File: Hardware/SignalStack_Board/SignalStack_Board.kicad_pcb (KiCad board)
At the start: 2 copper layers, 69.6 x 80.3 mm, 78 parts, among them J2 RJ45_LED_Shielded, J3 Molex_uF_SV_06, Q1 SI4156DY, Q2 SI4156DY, Q3 SI4156DY, Q4 SI4156DY, Q5 SI4156DY, Q6 SI4156DY, Q7 SI4156DY, Q8 SI4156DY, Q9 Q_PMOS_DGS, SW1 SW_Push, SW2 SW_Push, U1 OKI, U10 74LVC2G04, U2 SMAJ12CA, U3 Teensy4.1_DEV-16771, U4 TSR_1-2450, U5 IRS2005S, U6 IRS2005S, U7 74LVC2G04, U8 IRS2005S, U9 IRS2005S

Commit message: Rev3 schematic
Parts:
- added REF**: Arduino_UNO_R3, Module:Arduino_UNO_R3, B.Cu at (90.7, 106.6)
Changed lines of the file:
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@@
       ) (layer "B.SilkS") (width 0) (fill solid))
+  )
+  (footprint "Module:Arduino_UNO_R3" (layer "B.Cu")
+    (at 90.678 106.553 90)
+    (descr "Arduino UNO R3, http://www.mouser.com/pdfdocs/Gravitech_Arduino_Nano3_0.pdf")
+    (tags "Arduino UNO R3")
+    (attr through_hole)
+    (fp_text reference "REF**" (at 1.27 3.81 90) (layer "B.SilkS")
+      (effects (font (size 1 1) (thickness 0.15)) (justify mirror))
+    )
+    (fp_text value "Arduino_UNO_R3" (at 0 -22.86 90) (layer "B.Fab")
+      (effects (font (size 1 1) (thickness 0.15)) (justify mirror))
+    )
+    (fp_text user "${REFERENCE}" (at 0 -20.32 90) (layer "B.Fab")
+      (effects (font (size 1 1) (thickness 0.15)) (justify mirror))
+    )
+    (fp_line (start -28.07 -50.93) (end 36.58 -50.93) (layer "B.SilkS") (width 0.12))
+    (fp_line (start -28.07 -9.65) (end -28.07 -29.72) (layer "B.SilkS") (width 0.12))
+    (fp_line (start 38.23 -49.28) (end 38.23 -37.85) (layer "B.SilkS") (width 0.12))
+    (fp_line (start -29.97 -9.65) (end -28.07 -9.65) (layer "B.SilkS") (width 0.12))
+    (fp_line (start -34.42 -41.4) (end -28.07 -41.4) (layer "B.SilkS") (width 0.12))
+    (fp_line (start -28.07 -29.72) (end -34.42 -29.72) (layer "B.SilkS") (width 0.12))
+    (fp_line (start -34.42 -29.72) (end -34.42 -41.4) (layer "B.SilkS") (width 0.12))
+    (fp_line (start -28.07 -0.51) (end -29.97 -0.51) (layer "B.SilkS") (width 0.12))
+    (fp_line (start 38.23 2.67) (end -28.07 2.67) (layer "B.SilkS") (width 0.12))
+    (fp_line (start 38.23 -37.85) (end 40.77 -35.31) (layer "B.SilkS") (width 0.12))
+    (fp_line (start -29.97 -0.51) (end -29.97 -9.65) (layer "B.SilkS") (width 0.12))
+    (fp_line (start 40.77 -35.31) (end 40.77 -2.54) (layer "B.SilkS") (width 0.12))
+    (fp_line (start -28.07 -41.4) (end -28.07 -50.93) (layer "B.SilkS") (width 0.12))
+    (fp_line (start -28.07 2.67) (end -28.07 -0.51) (layer "B.SilkS") (width 0.12))
+    (fp_line (start 36.58 -50.93) (end 38.23 -49.28) (layer "B.SilkS") (width 0.12))
+    (fp_line (start 38.23 0) (end 38.23 2.67) (layer "B.SilkS") (width 0.12))
+    (fp_line (start 40.77 -2.54) (end 38.23 0) (layer "B.SilkS") (width 0.12))
+    (fp_line (start -30.1 -9.78) (end -30.1 -0.38) (layer "B.CrtYd") (width 0.05))
+    (fp_line (start -28.19 -9.78) (end -30.1 -9.78) (layer "B.CrtYd") (width 0.05))
+    (fp_line (start -28.19 2.79) (end 38.35 2.79) (layer "B.CrtYd") (width 0.05))
+    (fp_line (start 40.89 -35.31) (end 38.35 -37.85) (layer "B.CrtYd") (width 0.05))
+    (fp_line (start -28.19 -51.05) (end -28.19 -41.53) (layer "B.CrtYd") (width 0.05))
+    (fp_line (start -28.19 -0.38) (end -28.19 2.79) (layer "B.CrtYd") (width 0.05))
+    (fp_line (start -28.19 -29.59) (end -28.19 -9.78) (layer "B.CrtYd") (width 0.05))
+    (fp_line (start -34.54 -41.53) (end -34.54 -29.59) (layer "B.CrtYd") (width 0.05))
+    (fp_line (start -30.1 -0.38) (end -28.19 -0.38) (layer "B.CrtYd") (width 0.05))
+    (fp_line (start -28.19 -41.53) (end -34.54 -41.53) (layer "B.CrtYd") (width 0.05))
+    (fp_line (start 36.58 -51.05) (end -28.19 -51.05) (layer "B.CrtYd") (width 0.05))
+    (fp_line (start 38.35 -37.85) (end 38.35 -49.28) (layer "B.CrtYd") (width 0.05))
+    (fp_line (start 38.35 2.79) (end 38.35 0) (layer "B.CrtYd") (width 0.05))
+    (fp_line (start -34.54 -29.59) (end -28.19 -29.59) (layer "B.CrtYd") (width 0.05))
+    (fp_line (start 38.35 -49.28) (end 36.58 -51.05) (layer "B.CrtYd") (width 0.05))
+    (fp_line (start 40.89 -2.54) (end 40.89 -35.31) (layer "B.CrtYd") (width 0.05))
+    (fp_line (start 38.35 0) (end 40.89 -2.54) (layer "B.CrtYd") (width 0.05))
+    (fp_line (start 38.1 2.54) (end 38.1 0) (layer "B.Fab") (width 0.1))
+    (fp_line (start 40.64 -2.54) (end 40.64 -35.31) (layer "B.Fab") (width 0.1))
+    (fp_line (start -29.84 -0.64) (end -16.51 -0.64) (layer "B.Fab") (width 0.1))
+    (fp_line (start -16.51 -9.53) (end -29.84 -9.53) (layer "B.Fab") (width 0.1))
+    (fp_line (start -18.41 -29.84) (end -18.41 -41.27) (layer "B.Fab") (width 0.1))
+    (fp_line (start -29.84 -9.53) (end -29.84 -0.64) (layer "B.Fab") (width 0.1))
+    (fp_line (start 36.58 -50.8) (end -27.94 -50.8) (layer "B.Fab") (width 0.1))
+    (fp_line (start -16.51 -0.64) (end -16.51 -9.53) (layer "B.Fab") (width 0.1))
+    (fp_line (start -27.94 -50.8) (end -27.94 2.54) (layer "B.Fab") (width 0.1))
+    (fp_line (start -18.41 -41.27) (end -34.29 -41.27) (layer "B.Fab") (width 0.1))
+    (fp_line (start 38.1 -37.85) (end 38.1 -49.28) (layer "B.Fab") (width 0.1))
+    (fp_line (start 38.1 -49.28) (end 36.58 -50.8) (layer "B.Fab") (width 0.1))
+    (fp_line (start 38.1 0) (end 40.64 -2.54) (layer "B.Fab") (width 0.1))
+    (fp_line (start -34.29 -41.27) (end -34.29 -29.84) (layer "B.Fab") (width 0.1))
+    (fp_line (start 40.64 -35.31) (end 38.1 -37.85) (layer "B.Fab") (width 0.1))
+    (fp_line (start -27.94 2.54) (end 38.1 2.54) (layer "B.Fab") (width 0.1))
+    (fp_line (start -34.29 -29.84) (end -18.41 -29.84) (layer "B.Fab") (width 0.1))
+    (pad "1" thru_hole rect (at 0 0) (size 1.6 1.6) (drill 1) (layers *.Cu *.Mask))
+    (pad "2" thru_hole oval (at 2.54 0) (size 1.6 1.6) (drill 1) (layers *.Cu *.Mask))
+    (pad "3" thru_hole oval (at 5.08 0) (size 1.6 1.6) (drill 1) (layers *.Cu *.Mask))
+    (pad "4" thru_hole oval (at 7.62 0) (size 1.6 1.6) (drill 1) (layers *.Cu *.Mask))
+    (pad "5" thru_hole oval (at 10.16 0) (size 1.6 1.6) (drill 1) (layers *.Cu *.Mask))
+    (pad "6" thru_hole oval (at 12.7 0) (size 1.6 1.6) (drill 1) (layers *.Cu *.Mask))
+    (pad "7" thru_hole oval (at 15.24 0) (size 1.6 1.6) (drill 1) (layers *.Cu *.Mask))
+    (pad "8" thru_hole oval (at 17.78 0) (size 1.6 1.6) (drill 1) (layers *.Cu *.Mask))
+    (pad "9" thru_hole oval (at 22.86 0) (size 1.6 1.6) (drill 1) (layers *.Cu *.Mask))
+    (pad "10" thru_hole oval (at 25.4 0) (size 1.6 1.6) (drill 1) (layers *.Cu *.Mask))
+    (pad "11" thru_hole oval (at 27.94 0) (size 1.6 1.6) (drill 1) (layers *.Cu *.Mask))
+    (pad "12" thru_hole oval (at 30.48 0) (size 1.6 1.6) (drill 1) (layers *.Cu *.Mask))
+    (pad "13" thru_hole oval (at 33.02 0) (size 1.6 1.6) (drill 1) (layers *.Cu *.Mask))
+    (pad "14" thru_hole oval (at 35.56 0) (size 1.6 1.6) (drill 1) (layers *.Cu *.Mask))
+    (pad "15" thru_hole oval (at 35.56 -48.26) (size 1.6 1.6) (drill 1) (layers *.Cu *.Mask))
+    (pad "16" thru_hole oval (at 33.02 -48.26) (size 1.6 1.6) (drill 1) (layers *.Cu *.Mask))
+    (pad "17" thru_hole oval (at 30.48 -48.26) (size 1.6 1.6) (drill 1) (layers *.Cu *.Mask))
+    (pad "18" thru_hole oval (at 27.94 -48.26) (size 1.6 1.6) (drill 1) (layers *.Cu *.Mask))
+    (pad "19" thru_hole oval (at 25.4 -48.26) (size 1.6 1.6) (drill 1) (layers *.Cu *.Mask))
+    (pad "20" thru_hole oval (at 22.86 -48.26) (size 1.6 1.6) (drill 1) (layers *.Cu *.Mask))
+    (pad "21" thru_hole oval (at 20.32 -48.26) (size 1.6 1.6) (drill 1) (layers *.Cu *.Mask))
+    (pad "22" thru_hole oval (at 17.78 -48.26) (size 1.6 1.6) (drill 1) (layers *.Cu *.Mask))
+    (pad "23" thru_hole oval (at 13.72 -48.26) (size 1.6 1.6) (drill 1) (layers *.Cu *.Mask))
+    (pad "24" thru_hole oval (at 11.18 -48.26) (size 1.6 1.6) (drill 1) (layers *.Cu *.Mask))
+    (pad "25" thru_hole oval (at 8.64 -48.26) (size 1.6 1.6) (drill 1) (layers *.Cu *.Mask))
+    (pad "26" thru_hole oval (at 6.1 -48.26) (size 1.6 1.6) (drill 1) (layers *.Cu *.Mask))
+    (pad "27" thru_hole oval (at 3.56 -48.26) (size 1.6 1.6) (drill 1) (layers *.Cu *.Mask))
+    (pad "28" thru_hole oval (at 1.02 -48.26) (size 1.6 1.6) (drill 1) (layers *.Cu *.Mask))
+    (pad "29" thru_hole oval (at -1.52 -48.26) (size 1.6 1.6) (drill 1) (layers *.Cu *.Mask))
+    (pad "30" thru_hole oval (at -4.06 -48.26) (size 1.6 1.6) (drill 1) (layers *.Cu *.Mask))
+    (pad "31" thru_hole oval (at -6.6 -48.26) (size 1.6 1.6) (drill 1) (layers *.Cu *.Mask))
+    (pad "32" thru_hole oval (at -9.14 -48.26) (size 1.6 1.6) (drill 1) (layers *.Cu *.Mask))
+    (model "${KICAD6_3DMODEL_DIR}/Module.3dshapes/Arduino_UNO_R3.wrl"
+      (offset (xyz 0 0 0))
+      (scale (xyz 1 1 1))
+      (rotate (xyz 0 0 0))
+    )
   )
   (footprint "MRDT_Connectors:Square_Anderson_2_H_Side_By_Side" (layer "B.Cu")

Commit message: Made Rev3 layout
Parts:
- removed C6: 0.1uF, Capacitor_SMD:C_0603_1608Metric_Pad1.08x0.95mm_HandSolder
- removed the G*** at (159.8, 127.8)
- removed the G*** at (165.4, 104.9)
- removed J2: RJ45_LED_Shielded, MRDT_Connectors:RJ45_Teensy
- removed J3: Molex_uF_SV_06, Connector_Molex:Molex_SL_171971-0006_1x06_P2.54mm_Vertical
- removed R19, R20: 4.7k, Resistor_SMD:R_0603_1608Metric_Pad0.98x0.95mm_HandSolder
- removed REF**: Arduino_UNO_R3, Module:Arduino_UNO_R3
- removed U3: Teensy4.1_DEV-16771, MRDT_Shields:Teensy_4_1_Ethernet
- removed V4: Via, MRDT_Drill_Holes:4_40_Hole_Corner
- added A1: Arduino_UNO_R3, Module:Arduino_UNO_R3, F.Cu at (203.2, 34.3)
- added G***: LOGO, MRDT_Silkscreens:z_sig_Grant_Brinker_30mmx7.3, F.Cu at (202.6, 102.2)
- added G***: LOGO, MRDT_Silkscreens:zz_Helios_Logo_Short_3inx1.4in, F.Cu at (204.5, 61.6)
- C3: value 0.1uF -> 100uF; footprint Capacitor_SMD:C_0603_1608Metric_Pad1.08x0.95mm_HandSolder -> Capacitor_THT:CP_Radial_D6.3mm_P2.50mm
- C4: value 10uF -> 220uF; footprint Capacitor_SMD:C_0603_1608Metric_Pad1.08x0.95mm_HandSolder -> Capacitor_THT:CP_Radial_D6.3mm_P2.50mm
- C5: value 22uF -> 470uF; footprint Capacitor_SMD:C_0603_1608Metric_Pad1.08x0.95mm_HandSolder -> Capacitor_THT:CP_Radial_D10.0mm_P2.50mm
- U2: value SMAJ12CA -> Raspberry_Pi; footprint MRDT_Actives:DO-214AC -> MRDT_Shields:RaspberryPi_THT_BOTTOM
- moved V1 134.9 mm to (243.8, 108.0), turned to 90 degrees
- moved V3 120.5 mm to (125.7, 31.8), turned to -90 degrees
- moved C2 80.0 mm to (128.7, 59.3)
- moved V2 75.2 mm to (125.7, 108.0), turned to 0 degrees
- moved Conn1 69.5 mm to (231.8, 89.2)
- moved U1 60.4 mm to (134.6, 55.6), turned to 180 degrees
- moved D1 60.3 mm to (153.0, 47.8), turned to 180 degrees
- moved R1 59.7 mm to (149.2, 47.8), turned to 0 degrees
- moved Q9 59.1 mm to (221.3, 96.5), turned to 0 degrees
- moved U4 55.3 mm to (142.2, 50.8)
- moved C5 54.7 mm to (204.5, 92.7), turned to 90 degrees
- moved D3 54.7 mm to (153.0, 50.5), turned to 180 degrees
- moved C1 54.4 mm to (135.5, 59.3), turned to 0 degrees
- moved R3 54.1 mm to (149.2, 50.5), turned to 0 degrees
- moved D2 49.2 mm to (153.0, 53.3), turned to 180 degrees
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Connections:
- C3 pad 1: Net-(C3-Pad1) -> +12V
- C4 pad 1: Net-(C3-Pad1) -> +12V
- C5 pad 1: Net-(C3-Pad1) -> +12V
- Conn1 pad 2: Net-(C3-Pad1) -> Net-(Conn1-Pad2)
- D12 pad 1: +12V -> Net-(D12-Pad2)
- D12 pad 2: Net-(D12-Pad2) -> (no net)
- D12 pad 3: (no net) -> +12V
- Q9 pad 2: Net-(C3-Pad1) -> Net-(Conn1-Pad2)
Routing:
- net +3V3: track 293.6 -> 158.8 mm, vias 7 -> 4
- net GPS_TX1: track 0.00 -> 104.0 mm
- net Coil1_FWD: track 19.6 -> 117.8 mm
- net GPS_RX1: track 0.00 -> 91.6 mm
- net Coil2_RVS: track 16.5 -> 98.3 mm
- net Coil2_FWD: track 19.3 -> 96.3 mm
- net Coil1_RVS: track 19.4 -> 89.2 mm, vias 0 -> 2
- net I2C SCL: track 56.4 -> 0.00 mm, vias 1 -> 0
- net I2C SDA: track 53.3 -> 0.00 mm, vias 1 -> 0
- net +5V: track 53.9 -> 90.7 mm
- net /RX-: track 31.4 -> 0.00 mm
- net /RX+: track 31.4 -> 0.00 mm
- net /LED: track 31.1 -> 0.00 mm
- net /TX-: track 23.5 -> 0.00 mm
- net /TX+: track 23.5 -> 0.00 mm
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- added copper zone on F.Cu, net Net-(Conn1-Pad2)
- removed copper zone on F.Cu, net Net-(C3-Pad1)
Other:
- board size 69.6 x 80.3 mm -> 118.1 x 76.2 mm
- board text added: "3.3V"
- board text added: "Signal Stack Board, Rev3 Mars Rover Design Team Missouri S&T, 2023 Grant Brinker"
- board text removed: "3V3"
- board text removed: "Signal Stack Board, Rev 2 Mars Rover Design Team Missouri S&T, 2023 Grant Brinker"

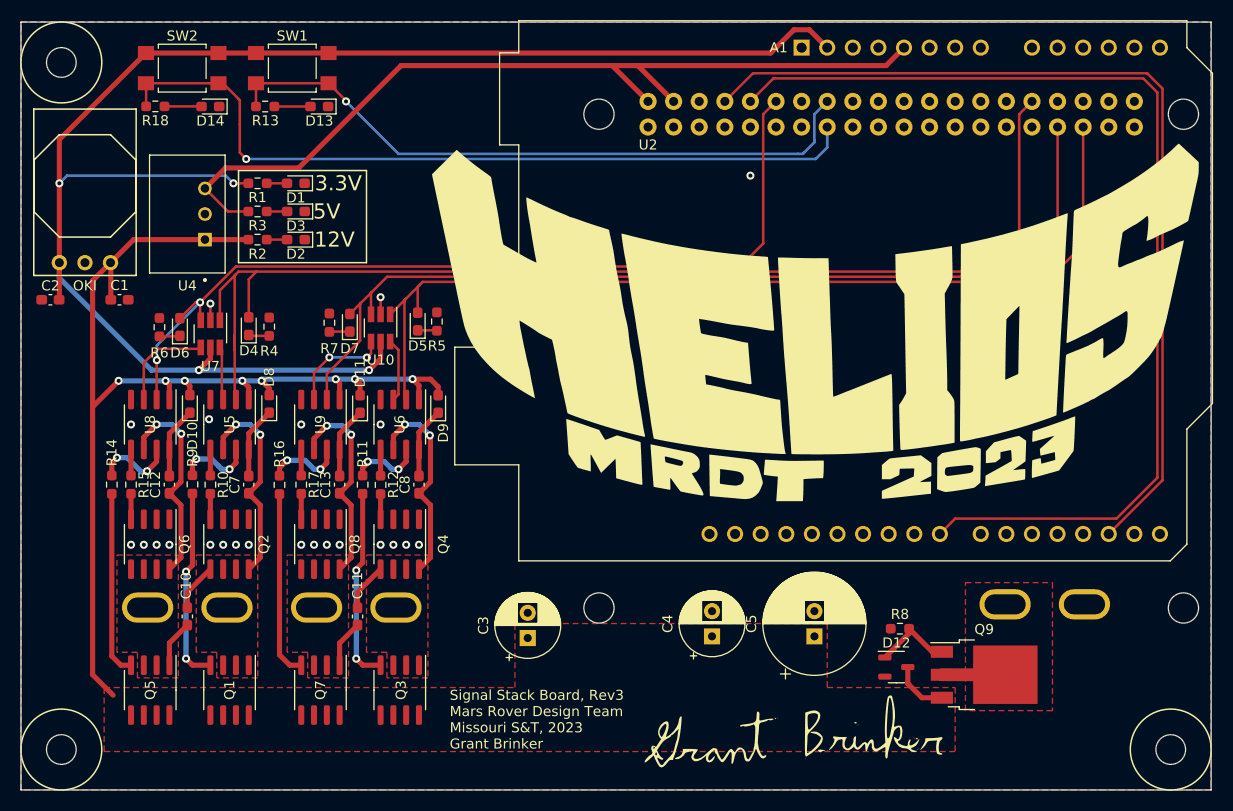
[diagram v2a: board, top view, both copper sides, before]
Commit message: Fixed edge cuts
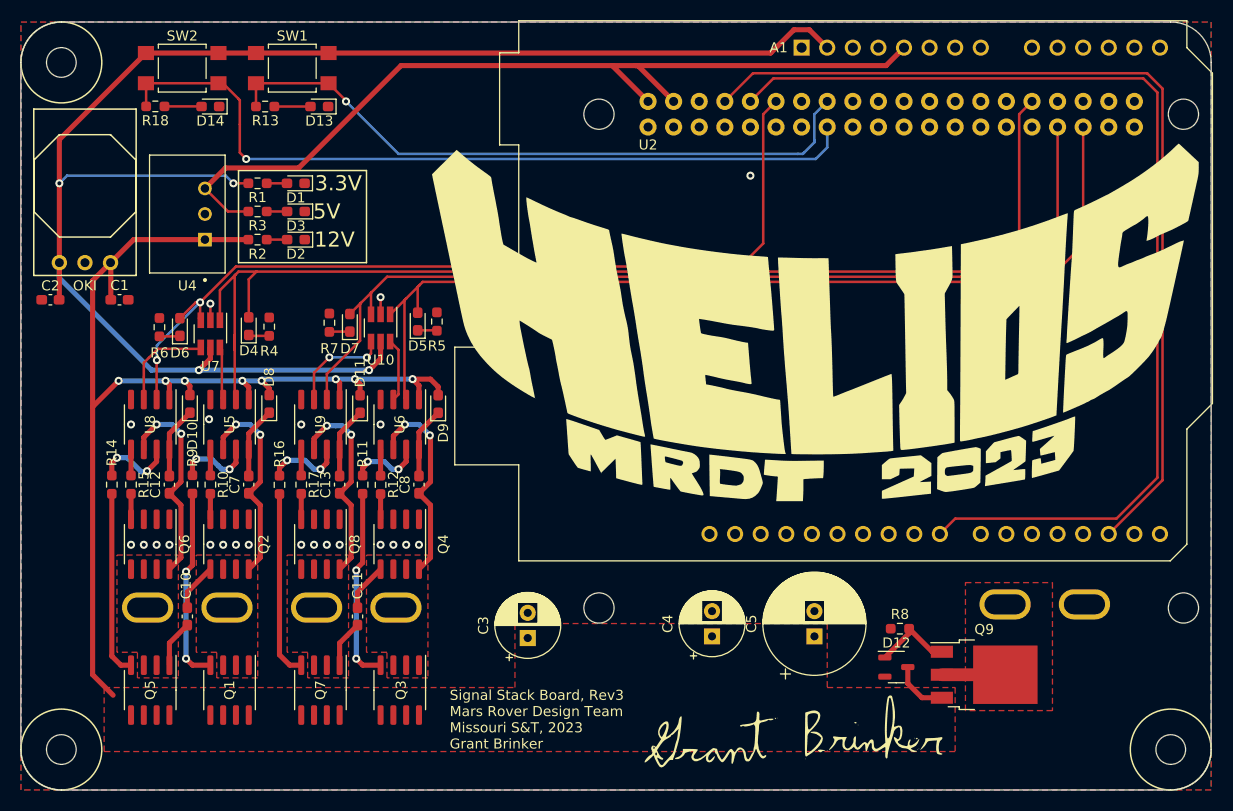
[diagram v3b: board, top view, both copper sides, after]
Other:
- outline, holes or cut-outs redrawn
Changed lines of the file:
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@@
   )
   (gr_rect (start 147.32 55.626) (end 160.02 46.482) (layer "F.SilkS") (width 0.15) (fill none))
-  (gr_rect (start 125.73 31.75) (end 243.84 107.95) (layer "Edge.Cuts") (width 0.1) (fill none))
+  (gr_line (start 243.84 103.9368) (end 243.847039 35.756161) (layer "Edge.Cuts") (width 0.1))
+  (gr_line (start 129.736161 31.742961) (end 239.833839 31.742961) (layer "Edge.Cuts") (width 0.1))
+  (gr_line (start 125.722961 103.943839) (end 125.722961 35.756161) (layer "Edge.Cuts") (width 0.1))
+  (gr_line (start 239.8268 107.95) (end 129.736161 107.957039) (layer "Edge.Cuts") (width 0.1))
+  (gr_arc (start 125.722961 35.756161) (mid 126.8984 32.9184) (end 129.736161 31.742961) (layer "Edge.Cuts") (width 0.1))
+  (gr_arc (start 239.833839 31.742961) (mid 242.6716 32.9184) (end 243.847039 35.756161) (layer "Edge.Cuts") (width 0.1))
+  (gr_arc (start 129.736161 107.957039) (mid 126.8984 106.7816) (end 125.722961 103.943839) (layer "Edge.Cuts") (width 0.1))
+  (gr_arc (start 243.84 103.9368) (mid 242.664561 106.774561) (end 239.8268 107.95) (layer "Edge.Cuts") (width 0.1))
   (gr_text "Signal Stack Board, Rev3\nMars Rover Design Team\nMissouri S&T, 2023\nGrant Brinker" (at 168.275 100.965) (layer "F.SilkS")
     (effects (font (size 1 1) (thickness 0.15)) (justify left))

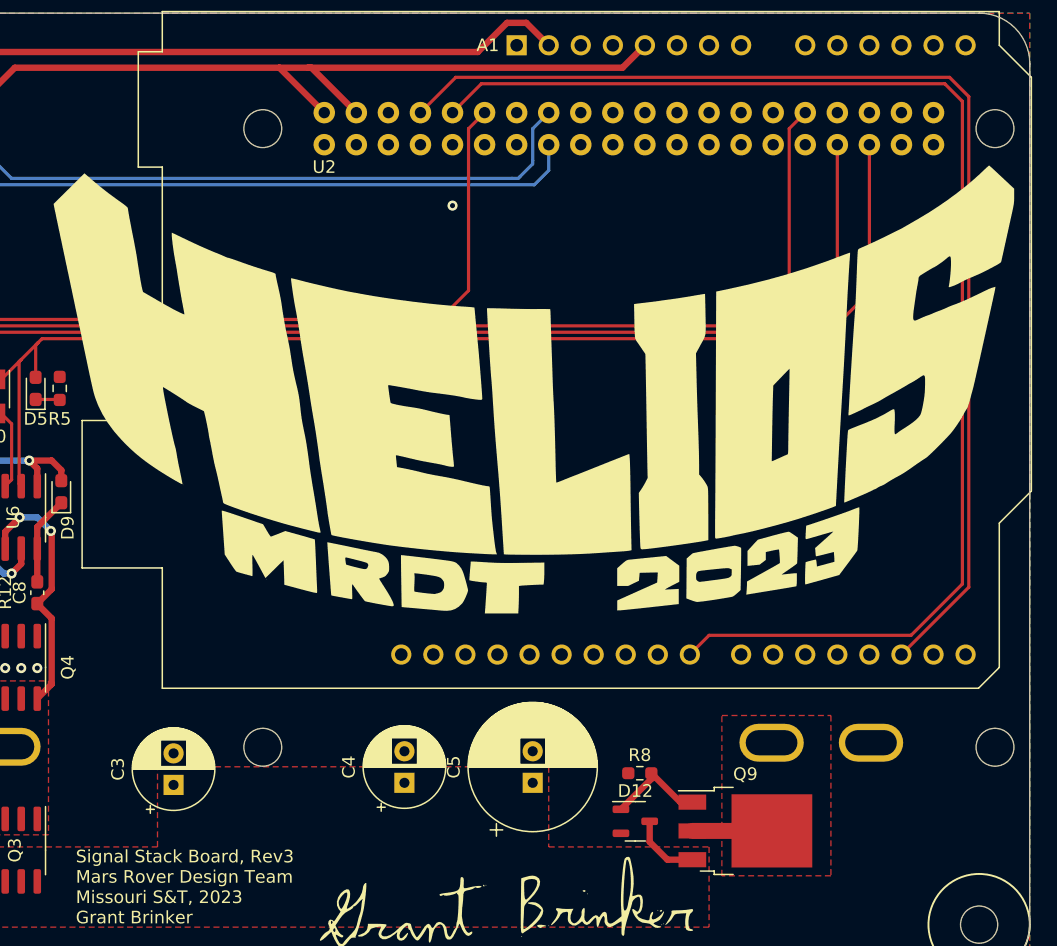
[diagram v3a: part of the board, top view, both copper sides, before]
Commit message: Added 2nd serial line
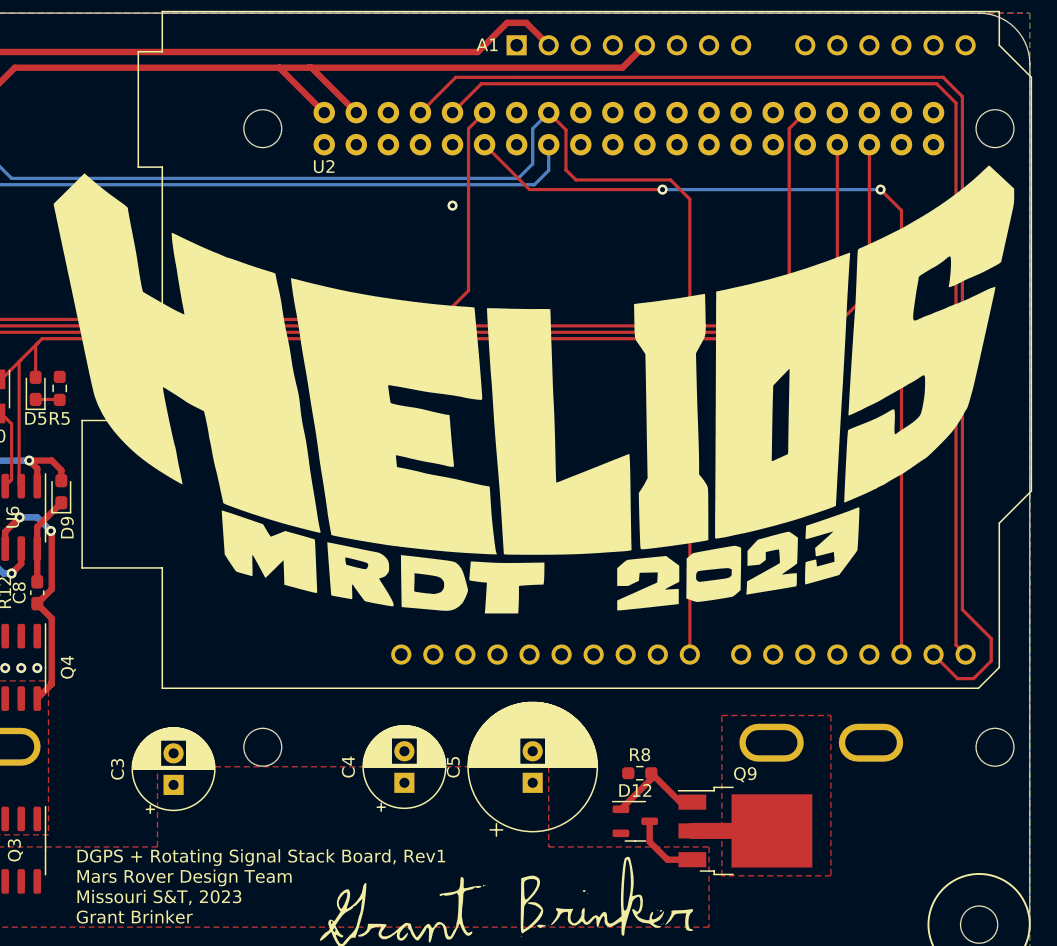
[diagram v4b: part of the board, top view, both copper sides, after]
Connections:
- A1 pad 15: unconnected-(A1-Pad15) -> GPS_TX1
- A1 pad 16: unconnected-(A1-Pad16) -> GPS_RX1
- A1 pad 17: GPS_RX1 -> GPS_TX2
- A1 pad 23: GPS_TX1 -> GPS_RX2
- U2 pad 11: unconnected-(U2-Pad11) -> GPS_TX2
- U2 pad 16: Motor 2 -> GPS_RX2
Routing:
- net GPS_TX2: track 0.00 -> 70.4 mm, vias 0 -> 2
- net GPS_RX2: track 0.00 -> 51.9 mm, vias 0 -> 2
- net GPS_TX1: track 104.0 -> 85.5 mm
- net GPS_RX1: track 91.6 -> 96.3 mm
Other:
- board text added: "DGPS + Rotating Signal Stack Board, Rev1 Mars Rover Design Team Missouri S&T, 2023 Grant Brinker"
- board text removed: "Signal Stack Board, Rev3 Mars Rover Design Team Missouri S&T, 2023 Grant Brinker"
